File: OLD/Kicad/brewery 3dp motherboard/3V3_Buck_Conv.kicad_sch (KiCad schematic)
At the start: 13 parts, among them J6 Conn_01x03_Pin, U2 LM61430AFSQRJRRQ1

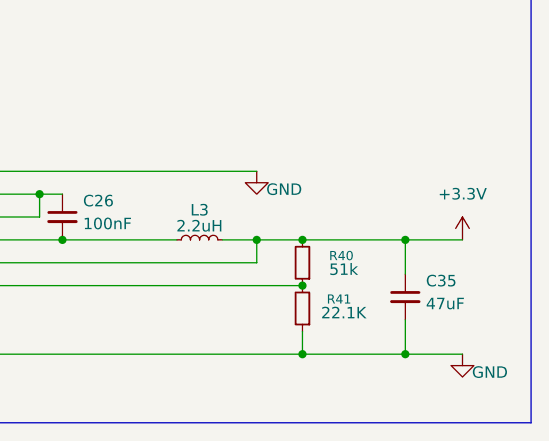
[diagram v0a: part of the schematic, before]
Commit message: cleaned up structure a bit
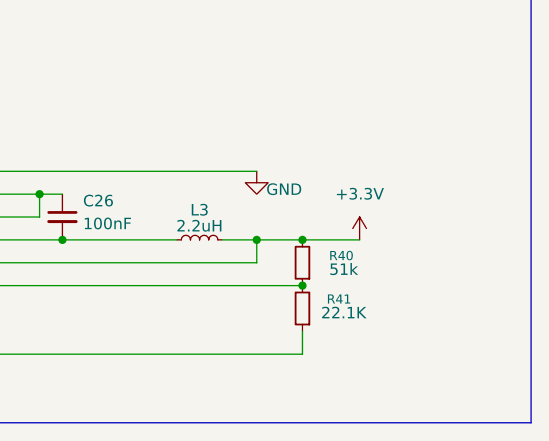
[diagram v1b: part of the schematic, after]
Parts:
- removed C35: 47uF, Capacitor_SMD:C_0805_2012Metric, symbol Device:C_Small
- C13, C14: footprint Capacitor_SMD:C_1206_3216Metric -> Capacitor_SMD:C_0402_1005Metric
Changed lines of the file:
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@@
+	)
+	(junction
+		(at 111.76 102.87)
+		(diameter 0)
+		(color 0 0 0 0)
+	)
+	(junction
+		(at 91.44 102.87)
+		(diameter 0)
+		(color 0 0 0 0)
+	)
+	(junction
+		(at 111.76 92.71)
+		(diameter 0)
+		(color 0 0 0 0)
+	)
+	(junction
+		(at 101.6 92.71)
+		(diameter 0)
+		(color 0 0 0 0)
+	)
+	(junction
+		(at 101.6 102.87)
+		(diameter 0)
+		(color 0 0 0 0)
+	)
+	(junction
+		(at 132.08 92.71)
+		(diameter 0)
+		(color 0 0 0 0)
+	)
+	(junction
+		(at 133.35 121.92)
+		(diameter 0)
+		(color 0 0 0 0)
+	)
+	(junction
+		(at 133.35 92.71)
+		(diameter 0)
+		(color 0 0 0 0)
+	)
+	(junction
+		(at 210.82 114.3)
+		(diameter 0)
+		(color 0 0 0 0)
+	)
+	(junction
+		(at 123.19 92.71)
+		(diameter 0)
+		(color 0 0 0 0)
+	)
+	(junction
+		(at 184.15 109.22)
+		(diameter 0)
+		(color 0 0 0 0)
 	)
 	(junction
@@
 	)
 	(junction
-		(at 111.76 102.87)
-		(diameter 0)
-		(color 0 0 0 0)
-	)
-	(junction
-		(at 222.25 121.92)
-		(diameter 0)
-		(color 0 0 0 0)
-	)
-	(junction
-		(at 91.44 102.87)
-		(diameter 0)
-		(color 0 0 0 0)
-	)
-	(junction
-		(at 111.76 92.71)
-		(diameter 0)
-		(color 0 0 0 0)
-	)
-	(junction
-		(at 101.6 92.71)
-		(diameter 0)
-		(color 0 0 0 0)
-	)
-	(junction
-		(at 101.6 102.87)
-		(diameter 0)
-		(color 0 0 0 0)
-	)
-	(junction
-		(at 132.08 92.71)
-		(diameter 0)
-		(color 0 0 0 0)
-	)
-	(junction
-		(at 133.35 121.92)
-		(diameter 0)
-		(color 0 0 0 0)
-	)
-	(junction
-		(at 133.35 92.71)
-		(diameter 0)
-		(color 0 0 0 0)
-	)
-	(junction
-		(at 210.82 114.3)
-		(diameter 0)
-		(color 0 0 0 0)
-	)
-	(junction
-		(at 123.19 92.71)
-		(diameter 0)
-		(color 0 0 0 0)
-	)
-	(junction
-		(at 184.15 109.22)
-		(diameter 0)
-		(color 0 0 0 0)
-	)
-	(junction
-		(at 222.25 109.22)
-		(diameter 0)
-		(color 0 0 0 0)
-	)
-	(junction
-		(at 210.82 121.92)
-		(diameter 0)
-		(color 0 0 0 0)
-	)
-	(junction
 		(at 91.44 92.71)
 		(diameter 0)
@@
 	(wire
 		(pts
-			(xy 222.25 118.11) (xy 222.25 121.92)
-		)
-		(stroke
-			(width 0)
-			(type default)
-		)
-	)
-	(wire
-		(pts
 			(xy 88.9 78.74) (xy 92.71 78.74)
 		)
@@
 	(wire
 		(pts
-			(xy 222.25 109.22) (xy 228.6 109.22)
-		)
-		(stroke
-			(width 0)
-			(type default)
-		)
-	)
-	(wire
-		(pts
 			(xy 171.45 104.14) (xy 181.61 104.14)
 		)
@@
 	(wire
 		(pts
-			(xy 222.25 121.92) (xy 228.6 121.92)
-		)
-		(stroke
-			(width 0)
-			(type default)
-		)
-	)
-	(wire
-		(pts
-			(xy 222.25 109.22) (xy 222.25 113.03)
-		)
-		(stroke
-			(width 0)
-			(type default)
-		)
-	)
-	(wire
-		(pts
 			(xy 171.45 101.6) (xy 205.74 101.6)
 		)
@@
 	(wire
 		(pts
-			(xy 210.82 121.92) (xy 222.25 121.92)
-		)
-		(stroke
-			(width 0)
-			(type default)
-		)
-	)
-	(wire
-		(pts
-			(xy 210.82 109.22) (xy 222.25 109.22)
+			(xy 210.82 109.22) (xy 217.17 109.22)
 		)
 		(stroke
@@
 	(symbol
 		(lib_id "Device:C_Small")
-		(at 222.25 115.57 0)
-		(unit 1)
-		(body_style 1)
-		(exclude_from_sim no)
-		(in_bom yes)
-		(on_board yes)
-		(in_pos_files yes)
-		(dnp no)
-		(property "Reference" "C35"
-			(at 224.536 113.792 0)
-			(show_name no)
-			(do_not_autoplace no)
-			(effects
-				(font
-					(size 1.27 1.27)
-				)
-				(justify left)
-			)
-		)
-		(property "Value" "47uF"
-			(at 224.536 116.332 0)
-			(show_name no)
-			(do_not_autoplace no)
-			(effects
-				(font
-					(size 1.27 1.27)
-				)
-				(justify left)
-			)
-		)
-		(property "Footprint" "Capacitor_SMD:C_0805_2012Metric"
-			(at 222.25 115.57 0)
-			(hide yes)
-			(show_name no)
-			(do_not_autoplace no)
-			(effects
-				(font
-					(size 1.27 1.27)
-				)
-			)
-		)
-		(property "Datasheet" ""
-			(at 222.25 115.57 0)
-			(hide yes)
-			(show_name no)
-			(do_not_autoplace no)
-			(effects
-				(font
-					(size 1.27 1.27)
-				)
-			)
-		)
-		(property "Description" "Unpolarized capacitor, small symbol"
-			(at 222.25 115.57 0)
-			(hide yes)
-			(show_name no)
-			(do_not_autoplace no)
-			(effects
-				(font
-					(size 1.27 1.27)
-				)
-			)
-		)
-		(pin "1"
-		)
-		(pin "2"
-		)
-		(instances
-			(project "brewery 3dp motherboard"
-				(path "/63771b13-dd98-4833-96bf-ef6b5d3ded40/0095169d-a3a6-414c-bad9-baaadd20e60a"
-					(reference "C35")
-					(unit 1)
-				)
-			)
-		)
-	)
-	(symbol
-		(lib_id "Device:C_Small")
 		(at 184.15 106.68 0)
 		(unit 1)
@@
 				(path "/63771b13-dd98-4833-96bf-ef6b5d3ded40/0095169d-a3a6-414c-bad9-baaadd20e60a"
 					(reference "C26")
-					(unit 1)
-				)
-			)
-		)
-	)
-	(symbol
-		(lib_id "power:GND")
-		(at 228.6 121.92 0)
-		(unit 1)
-		(body_style 1)
-		(exclude_from_sim no)
-		(in_bom yes)
-		(on_board yes)
-		(in_pos_files yes)
-		(dnp no)
-		(property "Reference" "#PWR038"
-			(at 228.6 128.27 0)
-			(hide yes)
-			(show_name no)
-			(do_not_autoplace no)
-			(effects
-				(font
-					(size 1.27 1.27)
-				)
-			)
-		)
-		(property "Value" "GND"
-			(at 231.648 123.952 0)
-			(show_name no)
-			(do_not_autoplace no)
-			(effects
-				(font
-					(size 1.27 1.27)
-				)
-			)
-		)
-		(property "Footprint" ""
-			(at 228.6 121.92 0)
-			(hide yes)
-			(show_name no)
-			(do_not_autoplace no)
-			(effects
-				(font
-					(size 1.27 1.27)
-				)
-			)
-		)
-		(property "Datasheet" ""
-			(at 228.6 121.92 0)
-			(hide yes)
-			(show_name no)
-			(do_not_autoplace no)
-			(effects
-				(font
-					(size 1.27 1.27)
-				)
-			)
-		)
-		(property "Description" "Power symbol creates a global label with name \"GND\" , ground"
-			(at 228.6 121.92 0)
-			(hide yes)
-			(show_name no)
-			(do_not_autoplace no)
-			(effects
-				(font
-					(size 1.27 1.27)
-				)
-			)
-		)
-		(pin "1"
-		)
-		(instances
-			(project "brewery 3dp motherboard"
-				(path "/63771b13-dd98-4833-96bf-ef6b5d3ded40/0095169d-a3a6-414c-bad9-baaadd20e60a"
-					(reference "#PWR038")
 					(unit 1)
 				)
@@
 			)
 		)
-		(property "Footprint" "Capacitor_SMD:C_1206_3216Metric"
+		(property "Footprint" "Capacitor_SMD:C_0402_1005Metric"
 			(at 111.76 97.79 0)
 			(hide yes)
@@
 	(symbol
 		(lib_id "power:+3.3V")
-		(at 228.6 109.22 0)
+		(at 217.17 109.22 0)
 		(unit 1)
 		(body_style 1)
@@
 		(fields_autoplaced yes)
 		(property "Reference" "#PWR032"
-			(at 228.6 113.03 0)
+			(at 217.17 113.03 0)
 			(hide yes)
 			(show_name no)
@@
 		)
 		(property "Value" "+3.3V"
-			(at 228.6 104.14 0)
+			(at 217.17 104.14 0)
 			(show_name no)
 			(do_not_autoplace no)
@@
 		)
 		(property "Footprint" ""
-			(at 228.6 109.22 0)
+			(at 217.17 109.22 0)
 			(hide yes)
 			(show_name no)
@@
 		)
 		(property "Datasheet" ""
-			(at 228.6 109.22 0)
+			(at 217.17 109.22 0)
 			(hide yes)
 			(show_name no)
@@
 		)
 		(property "Description" "Power symbol creates a global label with name \"+3.3V\""
-			(at 228.6 109.22 0)
+			(at 217.17 109.22 0)
 			(hide yes)
 			(show_name no)
@@
 			)
 		)
-		(property "Footprint" "Capacitor_SMD:C_1206_3216Metric"
+		(property "Footprint" "Capacitor_SMD:C_0402_1005Metric"
 			(at 123.19 97.79 0)
 			(hide yes)
